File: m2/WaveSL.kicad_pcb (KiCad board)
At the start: 4 copper layers, 55 x 20 mm, 40 parts, among them J1 SOICBite, J4 Screw_Terminal_01x02, U1 LED2000, U2 LPC812M001JDH16, U3 TPS7A0533PDBV, U4 LM75B

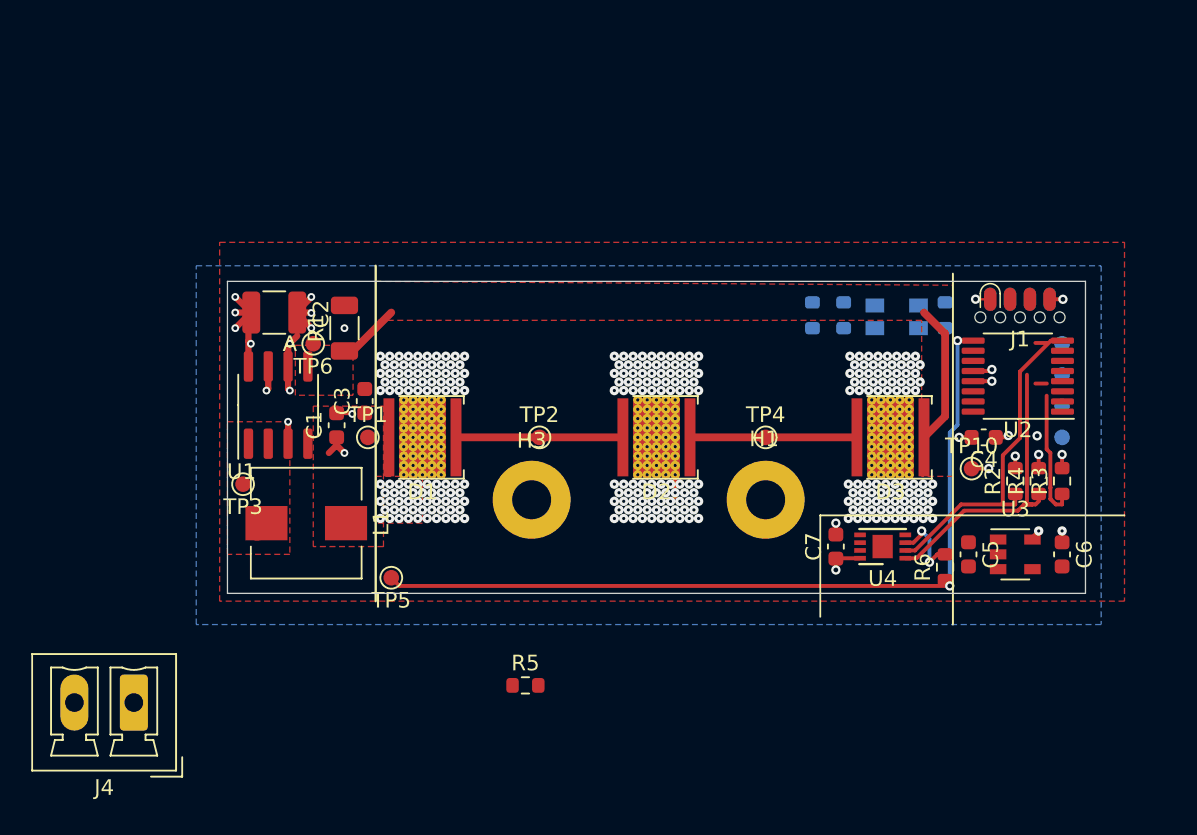
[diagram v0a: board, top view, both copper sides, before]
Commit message: tidy up silkscreen layer
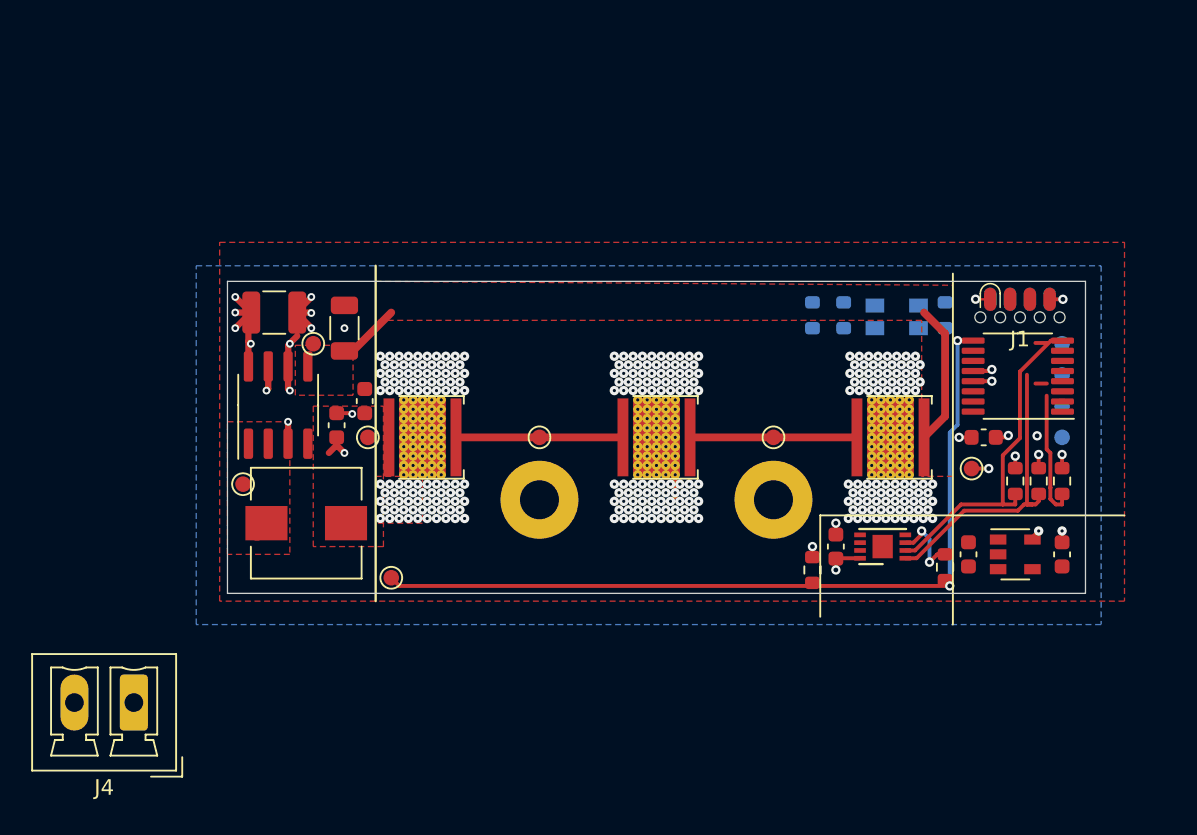
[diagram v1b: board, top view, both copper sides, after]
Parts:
- moved R5 19.8 mm to (174.0, 47.5), turned to 90 degrees
- moved H1 0.50 mm to (171.5, 43.0)
- moved H3 0.50 mm to (156.5, 43.0)
- moved TP4 0.50 mm to (171.5, 39.0)
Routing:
- net +3V3: track 10.4 -> 11.1 mm, vias 10 -> 11
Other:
- board text added: "WaveSL"
- board text added: "WaveSL m2r1"
- board text removed: "A"
- board text removed: "WaveACL m2r1"

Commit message: updates
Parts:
- removed H1: MountingHole, MountingHole:MountingHole_2.5mm_Pad
- J4: moved to B.Cu
- R7, R8, R9: moved to F.Cu
- moved J4 30.1 mm to (156.5, 40.8), turned to 90 degrees
- moved TP11 24.3 mm to (165.8, 30.4), turned to 270 degrees
- moved TP7 22.7 mm to (167.8, 30.4), turned to 270 degrees
- moved TP8 21.3 mm to (169.8, 30.4), turned to 270 degrees
- moved R7 20.4 mm to (190.5, 43.2), turned to 270 degrees
- moved TP9 20.1 mm to (171.8, 30.4), turned to 270 degrees
- moved R8 17.6 mm to (188.9, 43.2), turned to 270 degrees
- moved D4 17.4 mm to (187.9, 46.5), turned to 90 degrees
- moved H3 15.0 mm to (171.5, 43.1)
- moved R9 12.9 mm to (187.3, 43.2), turned to 270 degrees
- moved R2 2.26 mm to (187.5, 39.6)
- moved R3 2.26 mm to (190.5, 39.6), turned to 270 degrees
- moved R4 2.26 mm to (189.0, 39.6)
- moved C5 1.10 mm to (185.1, 46.6)
- moved U3 0.81 mm to (187.8, 46.6)
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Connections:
- J4 pad 1: Net-(J4-Pad1) -> GND
- J4 pad 2: Net-(J4-Pad2) -> VCC
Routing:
- net VCC: track 11.6 -> 65.5 mm, vias 6 -> 15
- net PWM: track 53.7 -> 67.5 mm
- net +3V3: track 11.1 -> 22.0 mm, vias 11 -> 9
- net /TXD: track 0.00 -> 10.3 mm, vias 0 -> 2
- net /RXD: track 0.00 -> 9.03 mm, vias 0 -> 2
- net /SWCLK: track 0.00 -> 8.14 mm, vias 0 -> 1
- net /GPIO: track 0.00 -> 7.58 mm, vias 0 -> 1
- net /~RESET: track 9.02 -> 15.2 mm, vias 0 -> 1
- net /SWDIO: track 0.00 -> 5.10 mm, vias 0 -> 1
- net GND: track 18.0 -> 22.1 mm, vias 293 -> 300
- net /SDA: track 19.2 -> 20.9 mm, vias 0 -> 2
- net /LED-: track 13.1 -> 14.5 mm
- net /LED_G: track 0.00 -> 1.20 mm, vias 0 -> 1
- net /SCK: track 22.2 -> 21.9 mm, vias 0 -> 2
- added copper zone on B.Cu, net VCC
- added copper zone on F.Cu, net VCC
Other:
- net class Default: via_dia 0.8 -> 0.6; via_drill 0.4 -> 0.3

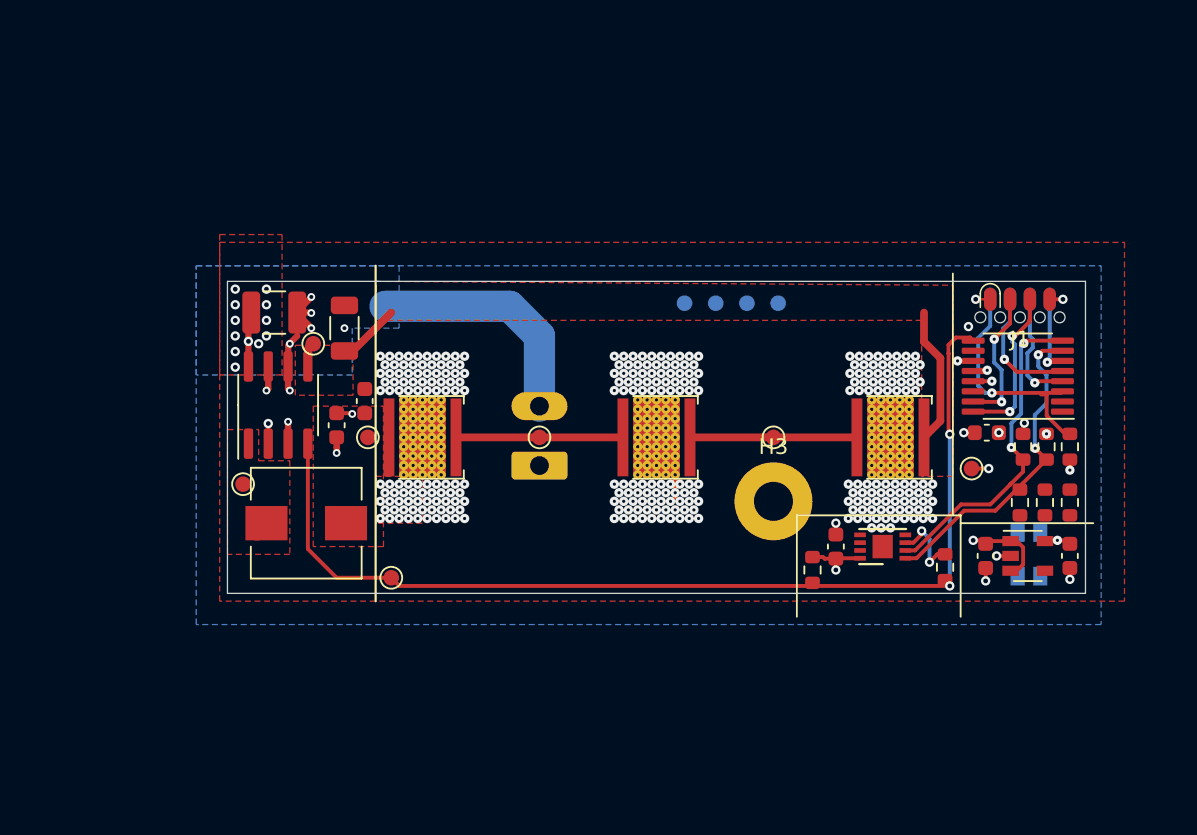
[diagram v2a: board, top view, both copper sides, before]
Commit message: updates
- LMZM23600V3SIL for 3.3 V
- AAA3528SEEZGKQBKS as status LED
- pads for VIN
- …
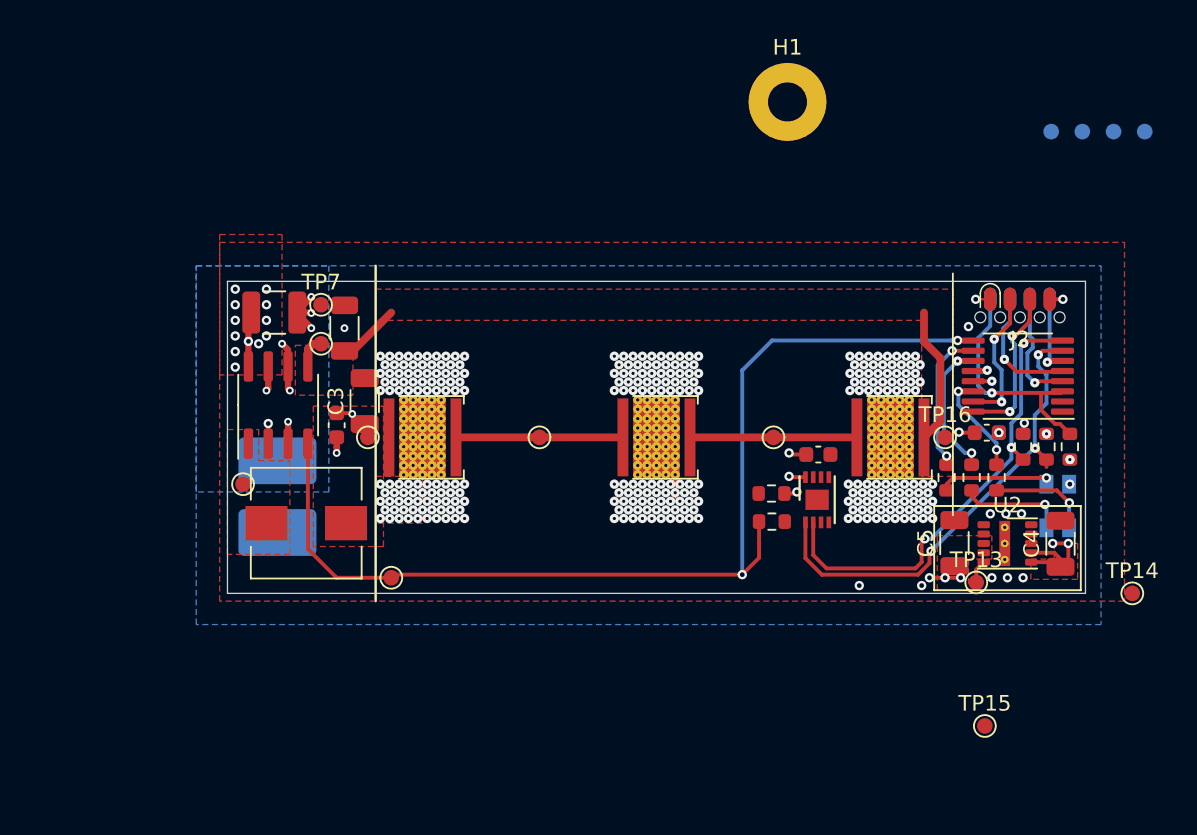
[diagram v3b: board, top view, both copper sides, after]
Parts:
- removed C6: 100n, Capacitor_SMD:C_0603_1608Metric
- removed the TP10 at (184.2, 41.0)
- removed U3: TPS7A0533PDBV, Package_TO_SOT_SMD:SOT-23-5
- added C4: 33u, Capacitor_SMD:C_1206_3216Metric, F.Cu at (189.9, 45.8)
- added TP13: TestPoint, TestPoint:TestPoint_Pad_D1.0mm, F.Cu at (184.5, 48.3)
- added TP14: TestPoint, TestPoint:TestPoint_Pad_D1.0mm, F.Cu at (194.5, 49.0)
- added TP15: TestPoint, TestPoint:TestPoint_Pad_D1.0mm, F.Cu at (185.1, 57.5)
- added TP16: TestPoint, TestPoint:TestPoint_Pad_D1.0mm, F.Cu at (182.5, 39.0)
- added TP7: TestPoint, TestPoint:TestPoint_Pad_D1.0mm, F.Cu at (142.5, 30.5)
- added U2: LMZM23600V3, Package_LGA:Texas_SIL0010A_MicroSiP-10-1EP_3.8x3mm_P0.6mm_EP0.7x2.9mm_ThermalVias, F.Cu at (186.5, 45.8)
- C3: footprint Capacitor_SMD:C_0603_1608Metric -> Capacitor_SMD:C_1206_3216Metric
- C5: value 100n -> 10u 50V; footprint Capacitor_SMD:C_0603_1608Metric -> Capacitor_SMD:C_1206_3216Metric
- D4: value LED_RABG -> AAA3528SEEZGKQBKS; footprint LED_SMD:LED_Kingbright_AAA3528ESGCT -> fkl-footprints:LED_Kingbright_AAA3528SEEZGKQBKS
- J1: renamed from J4; footprint Connector_Phoenix_MC:PhoenixContact_MCV_1,5_2-G-3.81_1x02_P3.81mm_Vertical -> fkl-footprints:SolderWire-foo
- moved TP10 25.9 mm to (189.3, 19.4)
- moved TP12 25.9 mm to (195.3, 19.4)
- moved TP8 25.9 mm to (191.3, 19.4)
- moved TP9 25.9 mm to (193.3, 19.4)
- moved H1 25.6 mm to (172.4, 17.5)
- moved J1 16.8 mm to (139.7, 40.5), turned to 270 degrees
- moved R9 11.5 mm to (171.4, 44.4), turned to 0 degrees
- moved C9 6.01 mm to (174.4, 40.1), turned to 0 degrees
- moved R5 5.56 mm to (171.4, 42.6), turned to 0 degrees
- moved U4 5.16 mm to (174.3, 43.0), turned to 90 degrees
- moved R3 4.96 mm to (184.2, 41.6)
- moved R4 4.96 mm to (182.6, 41.6)
- moved R2 4.96 mm to (185.8, 41.6)
- moved D4 3.61 mm to (189.7, 43.4)
- moved C5 2.16 mm to (183.1, 45.8), turned to 90 degrees
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- renumbered C2 to C1, C1 to C2, C4 to C8, C7 to C9, H3 to H1, J1 to J2, R7 to R2, R8 to R3, R9 to R4, R2 to R6, R4 to R7, R3 to R8, R6 to R9, TP11 to TP10, TP9 to TP12, TP5 to TP4, TP6 to TP5, TP4 to TP6, TP7 to TP8, TP8 to TP9, U2 to U5
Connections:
- D4 pad 2: GND -> +3V3
- J1 pad 1: GND -> VCC
- J1 pad 2: VCC -> GND
- TP10 pad 1: GND -> +3V3
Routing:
- net +3V3: track 22.0 -> 32.8 mm, vias 9 -> 12
- net /SDA: track 20.9 -> 30.9 mm, vias 2 -> 3
- net /LED_B: track 0.00 -> 9.27 mm, vias 0 -> 2
- net /SCK: track 21.9 -> 30.9 mm, vias 2 -> 3
- net /LED_G: track 1.20 -> 9.20 mm, vias 1 -> 2
- net Net-(D4-Pad3): track 0.00 -> 7.37 mm, vias 0 -> 1
- net Net-(D4-Pad4): track 0.00 -> 7.15 mm, vias 0 -> 1
- net /LED_R: track 0.00 -> 6.66 mm, vias 0 -> 2
- net Net-(D4-Pad1): track 0.00 -> 6.61 mm, vias 0 -> 1
- net GND: track 22.1 -> 16.8 mm, vias 300 -> 301
- net VCC: track 65.5 -> 60.5 mm, vias 15 -> 17
- net Net-(R9-Pad2): track 4.90 -> 0.00 mm, vias 2 -> 0
- net PWM: track 67.5 -> 68.6 mm
- net Net-(TP13-Pad1): track 0.00 -> 1.00 mm
- added copper zone on F.Cu, net +3V3
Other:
- board text removed: "WaveSL"

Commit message: updates
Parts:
- removed H1: MountingHole_Pad, MountingHole:MountingHole_2.5mm_Pad
- removed TP10, TP12, TP14, TP15, TP8, TP9: TestPoint, TestPoint:TestPoint_Pad_D1.0mm
- C1: footprint Capacitor_SMD:C_1210_3225Metric -> Capacitor_SMD:C_1206_3216Metric
- C5: value 10u 50V -> 10u
- D1, D2, D3: value LED -> XMLBWT-00-0000-0000T5051
- L1: value 2.2u -> 3.3u
- R1: value R -> 0R05
- U1: value LED2000 -> LED2000DR
- U2: value LMZM23600V3 -> LMZM23600V3SILR
- moved TP1 1.00 mm to (145.5, 40.0)
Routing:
- net PWM: track 68.6 -> 71.7 mm
- net VCC: track 60.5 -> 61.7 mm, vias 17 -> 23
- net /LED+: track 0.00 -> 1.00 mm
- net GND: track 16.8 -> 16.5 mm, vias 301 -> 339
- added copper zone on F.Cu, net Net-(D1-Pad1)
- added copper zone on F.Cu, net Net-(D2-Pad1)
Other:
- board text added: "+"
- board text added: "-"
- board text added: "github.com/fb/WaveSL m2r1"
- board text removed: "WaveSL m2r1"

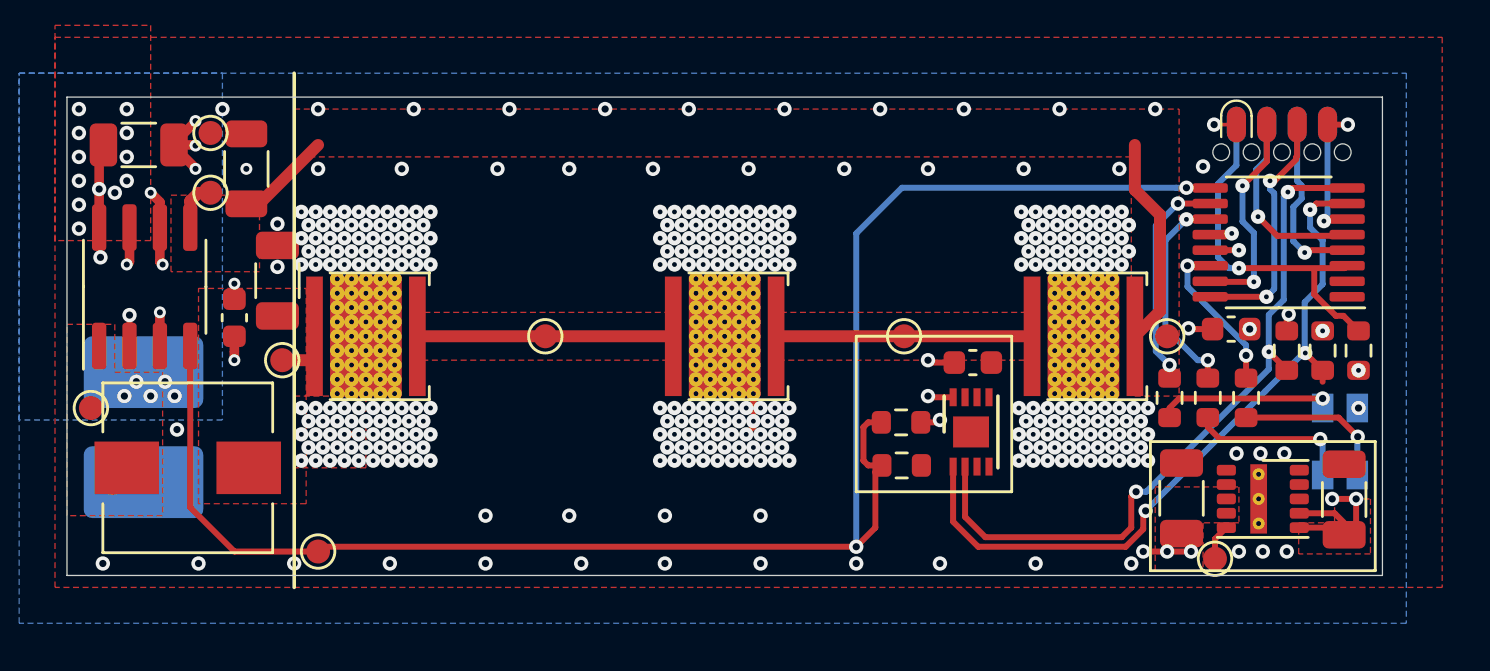
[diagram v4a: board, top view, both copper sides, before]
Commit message: update footprints and add U3 sensor
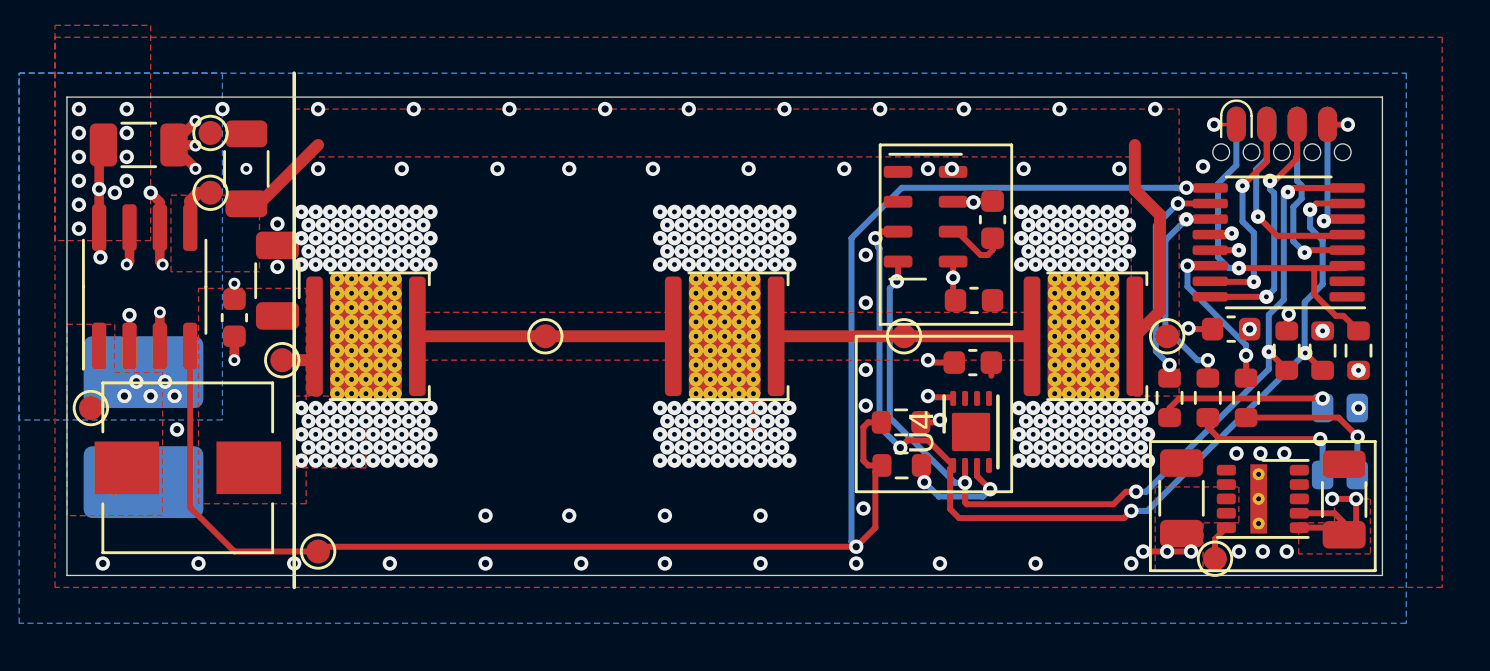
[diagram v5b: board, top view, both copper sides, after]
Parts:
- added C6: 100n, Capacitor_SMD:C_0603_1608Metric, F.Cu at (175.2, 34.1)
- added C7: 100n, Capacitor_SMD:C_0603_1608Metric, F.Cu at (174.4, 37.5)
- added U3: MPL3115A2, Package_LGA:NXP_LGA-8_3x5mm_P1.25mm_H1.1mm, F.Cu at (172.4, 34.0)
- U4: value LM75B -> LM75BTP; footprint Package_DFN_QFN:DFN-8-1EP_3x2mm_P0.5mm_EP1.3x1.5mm -> fkl-footprints:HWSON-8-1EP_3x2mm_P0.5mm_EP1.6x1.6mm
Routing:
- net /SDA: track 30.9 -> 42.0 mm, vias 3 -> 5
- net +3V3: track 32.8 -> 43.1 mm, vias 12 -> 14
- net /SCK: track 30.9 -> 39.6 mm, vias 3 -> 5
- net Net-(R9-Pad2): track 0.00 -> 5.10 mm, vias 0 -> 2
- net Net-(C6-Pad2): track 0.00 -> 2.64 mm
- net GND: track 16.5 -> 18.7 mm, vias 339 -> 345
